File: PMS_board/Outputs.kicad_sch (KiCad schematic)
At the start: 92 parts, among them J10 AUX1, J11 AUX2, J12 D1, J13 D2, J14 D3, J15 D4, J16 T1, J17 T2, J18 T3, J19 T4, J4 Chopper_Shunt, J5 CORE, J6 DRIVE, J7 JET1, J8 JET2, J9 NET, Q5 NMOS, Q6 NMOS, U10 VN7140ASTR, U11 VN7140ASTR, U12 VN7140ASTR, U13 VN7007AHTR, U14 VN7007AHTR, U15 LM74700, U16 TLV7011DCKR, U17 LT1910, U19 LM74700, U25 IRFS7530TRL7PP

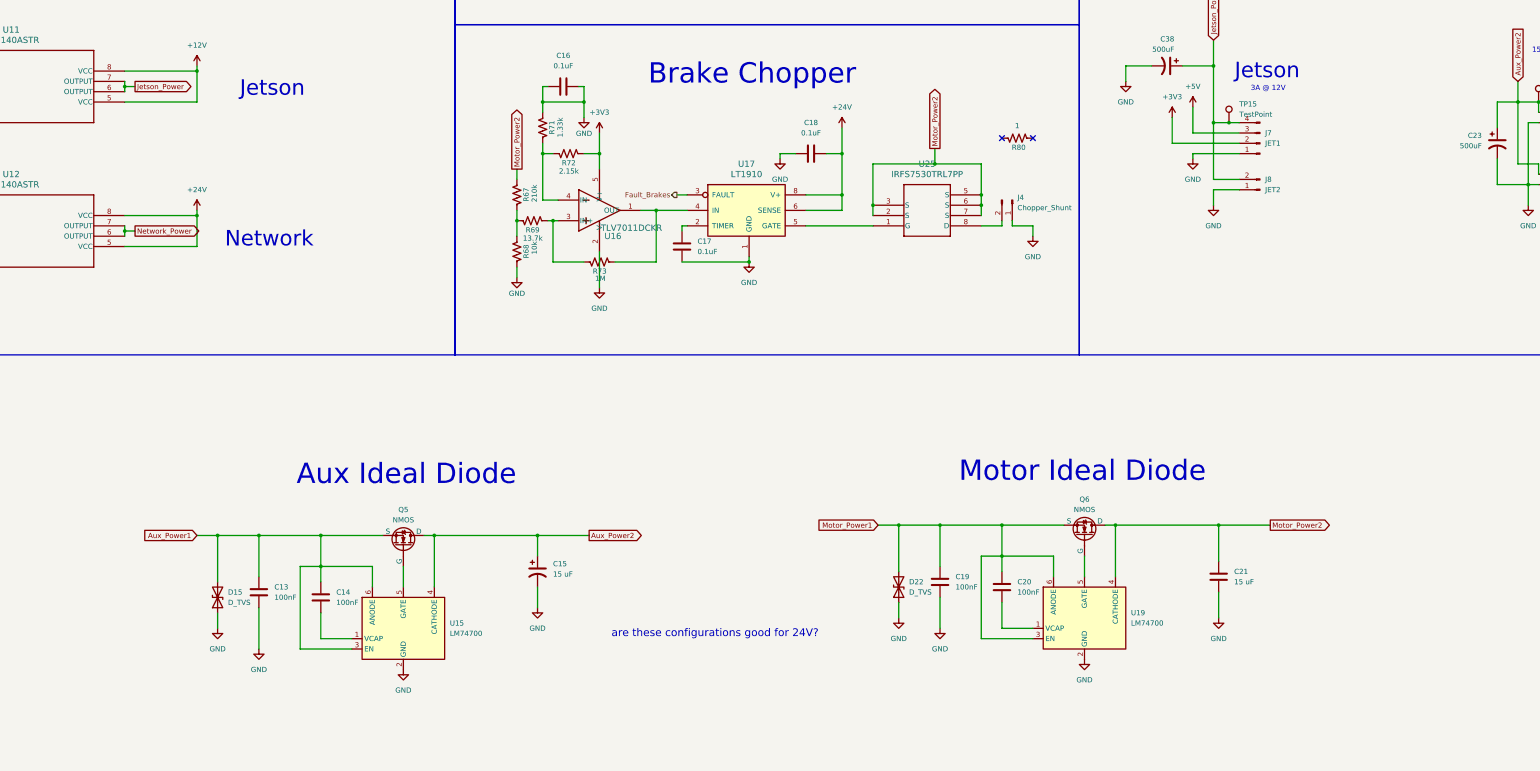
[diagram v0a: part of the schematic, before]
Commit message: Add pins to STM Chip
I also changed chips for jetson and motor out.
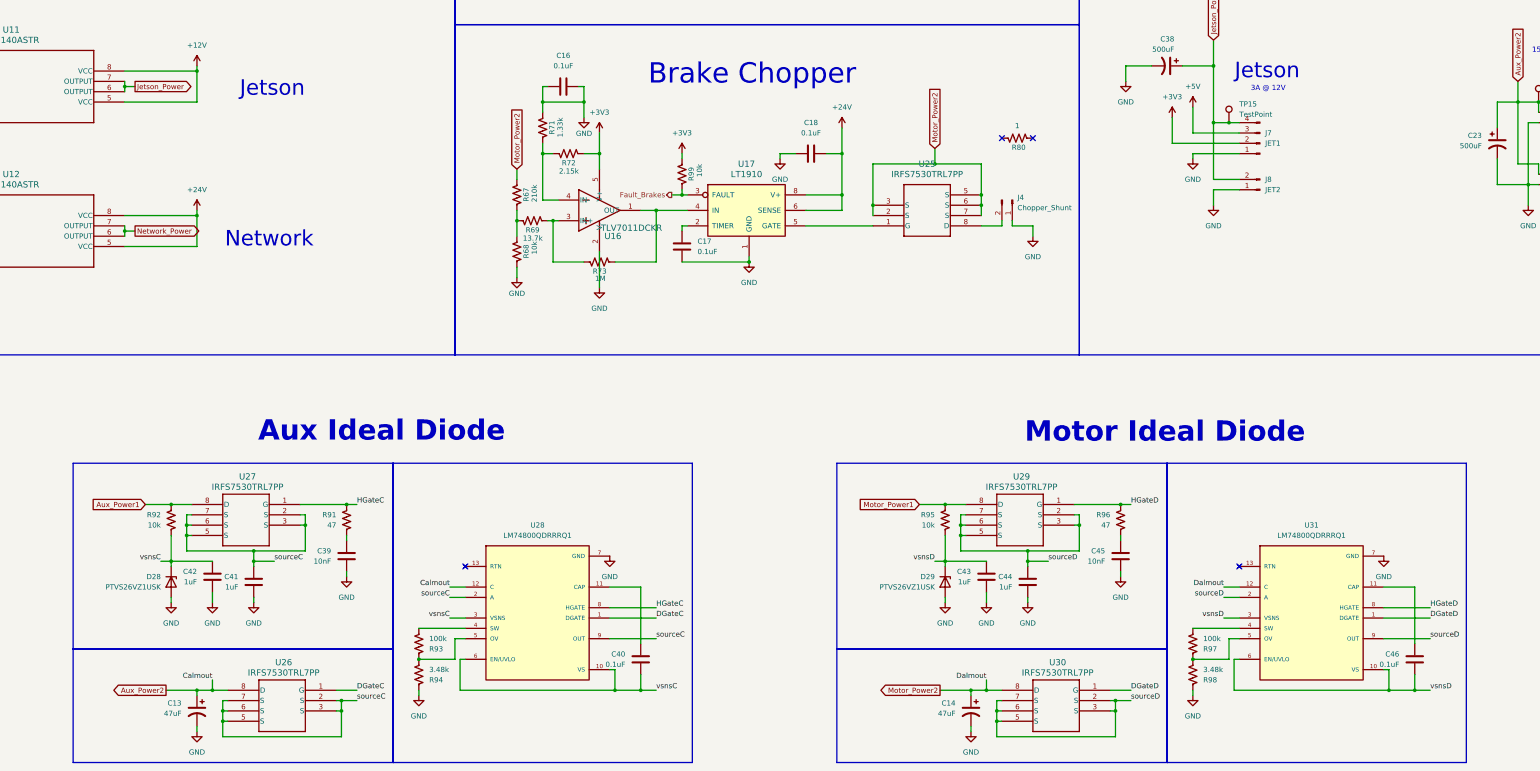
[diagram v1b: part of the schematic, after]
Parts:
- removed C13, C19: 100nF, Capacitor_SMD:C_0603_1608Metric, symbol Device:C
- removed C14, C20: 100nF, Capacitor_SMD:C_0603_1608Metric_Pad1.08x0.95mm_HandSolder, symbol Device:C
- removed C15: 15 uF, Capacitor_SMD:C_0603_1608Metric_Pad1.08x0.95mm_HandSolder, symbol Device:C_Polarized_US
- removed C21: 15 uF, Capacitor_SMD:C_0603_1608Metric_Pad1.08x0.95mm_HandSolder, symbol Device:C
- removed D15, D22: D_TVS, Diode_SMD:D_SOD-323_HandSoldering, symbol Device:D_TVS
- removed Q5, Q6: NMOS, Package_DFN_QFN:Nordic_AQFN-94-1EP_7x7mm_P0.4mm, symbol Simulation_SPICE:NMOS
- removed U15, U19: LM74700, Package_TO_SOT_SMD:SOT-23-6, symbol Power_Management:LM74700
- added C13, C14: 47uF, Capacitor_SMD:C_0603_1608Metric_Pad1.08x0.95mm_HandSolder, symbol Device:C_Polarized_US
- added C39, C45: 10nF, Capacitor_SMD:C_0603_1608Metric_Pad1.08x0.95mm_HandSolder, symbol Device:C
- added C40, C46: 0.1uF, Capacitor_SMD:C_0603_1608Metric_Pad1.08x0.95mm_HandSolder, symbol Device:C
- added C41, C42, C43, C44: 1uF, Capacitor_SMD:C_0603_1608Metric_Pad1.08x0.95mm_HandSolder, symbol Device:C
- added D28, D29: PTVS26VZ1USK, Diode_SMD:Nexperia_DSN1608-2_1.6x0.8mm, symbol Diode:PTVS26VZ1USK
- added R91, R96: 47, Resistor_SMD:R_0603_1608Metric_Pad0.98x0.95mm_HandSolder, symbol Device:R_US
- added R92, R95, R99: 10k, Resistor_SMD:R_0603_1608Metric_Pad0.98x0.95mm_HandSolder, symbol Device:R_US
- added R93, R97: 100k, Resistor_SMD:R_0603_1608Metric_Pad0.98x0.95mm_HandSolder, symbol Device:R_US
- added R94, R98: 3.48k, Resistor_SMD:R_0603_1608Metric_Pad0.98x0.95mm_HandSolder, symbol Device:R_US
- added U26, U27, U29, U30: IRFS7530TRL7PP, IRFS7530TRL7PP:PG-TO263-7_INF, symbol IRFS7530TRL7PP:IRFS7530TRL7PP
- added U28, U31: LM74800QDRRRQ1, LM74800QDRRRQ1:IC_LM74800QDRRRQ1, symbol LM74800QDRRRQ1:LM74800QDRRRQ1
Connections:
- net +3V3: now also R99.2
- net Aux_Power1: now also R92.2, U27.8 (D)
- net Aux_Power2: now also C13.1, U26.8 (D), U28.12 (C)
- net Fault_Brakes: now also R99.1
- net GND: now also C13.2, C14.2, C39.2, C41.2, C42.2, C43.2, C44.2, C45.2, D28.2 (A), D29.2 (A), R94.1, R98.1, U28.7 (GND), U31.7 (GND)
- net Motor_Power1: now also R95.2, U29.8 (D)
- net Motor_Power2: now also C14.1, U30.8 (D), U31.12 (C)
- new net: C40.1, U28.11 (CAP)
- new net: R93.2, U28.4 (SW)
- new net: R93.1, R94.2, U28.5 (OV)
- new net: C39.1, R91.2
- new net: R97.1, R98.2, U31.5 (OV)
- new net: R97.2, U31.4 (SW)
- new net: C46.1, U31.11 (CAP)
- new net: C45.1, R96.2
- new net DGateC: U26.1 (G), U28.1 (DGATE)
- new net DGateD: U30.1 (G), U31.1 (DGATE)
- new net HGateC: R91.1, U27.1 (G), U28.8 (HGATE)
- new net HGateD: R96.1, U29.1 (G), U31.8 (HGATE)
- new net sourceC: C41.1, U26.2 (S), U26.3 (S), U26.5 (S), U26.6 (S), U26.7 (S), U27.2 (S), U27.3 (S), U27.5 (S), U27.6 (S), U27.7 (S), U28.2 (A), U28.9 (OUT)
- new net sourceD: C44.1, U29.2 (S), U29.3 (S), U29.5 (S), U29.6 (S), U29.7 (S), U30.2 (S), U30.3 (S), U30.5 (S), U30.6 (S), U30.7 (S), U31.2 (A), U31.9 (OUT)
- new net vsnsC: C40.2, C42.1, D28.1 (K), R92.1, U28.10 (VS), U28.3 (VSNS), U28.6 (EN/UVLO)
- new net vsnsD: C43.1, C46.2, D29.1 (K), R95.1, U31.10 (VS), U31.3 (VSNS), U31.6 (EN/UVLO)
- no-connect marks 2 -> 4
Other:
- note removed: "are these configurations good for 24V?"

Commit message: Fix resistor value
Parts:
- R99: value 10k -> 4.7k
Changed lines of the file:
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@@
 			)
 		)
-		(property "Value" "10k"
+		(property "Value" "4.7k"
 			(at 278.638 170.18 90)
 			(show_name no)

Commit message: Schmitt Trigger
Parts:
- R67: value 210k -> 221k
- R69: value 13.7k -> 60.4k
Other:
- moved on the sheet: C14, U30
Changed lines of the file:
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@@
 	)
 	(junction
-		(at 381 304.8)
+		(at 379.73 304.8)
 		(diameter 0)
 		(color 0 0 0 0)
@@
 	)
 	(junction
-		(at 349.25 299.72)
+		(at 347.98 299.72)
 		(diameter 0)
 		(color 0 0 0 0)
@@
 	)
 	(junction
-		(at 345.44 299.72)
+		(at 344.17 299.72)
 		(diameter 0)
 		(color 0 0 0 0)
@@
 	)
 	(junction
-		(at 381 302.26)
+		(at 379.73 302.26)
 		(diameter 0)
 		(color 0 0 0 0)
@@
 	)
 	(junction
-		(at 351.79 304.8)
+		(at 350.52 304.8)
 		(diameter 0)
 		(color 0 0 0 0)
@@
 	)
 	(junction
-		(at 351.79 307.34)
+		(at 350.52 307.34)
 		(diameter 0)
 		(color 0 0 0 0)
@@
 	(wire
 		(pts
-			(xy 351.79 307.34) (xy 351.79 311.15)
+			(xy 350.52 307.34) (xy 350.52 311.15)
 		)
 		(stroke
@@
 	(wire
 		(pts
-			(xy 381 304.8) (xy 379.73 304.8)
+			(xy 379.73 304.8) (xy 378.46 304.8)
 		)
 		(stroke
@@
 	(wire
 		(pts
-			(xy 349.25 299.72) (xy 353.06 299.72)
+			(xy 347.98 299.72) (xy 351.79 299.72)
 		)
 		(stroke
@@
 	(wire
 		(pts
-			(xy 381 302.26) (xy 381 304.8)
+			(xy 379.73 302.26) (xy 379.73 304.8)
 		)
 		(stroke
@@
 	(wire
 		(pts
-			(xy 384.81 299.72) (xy 379.73 299.72)
+			(xy 383.54 299.72) (xy 378.46 299.72)
 		)
 		(stroke
@@
 	(wire
 		(pts
-			(xy 381 304.8) (xy 381 311.15)
+			(xy 379.73 304.8) (xy 379.73 311.15)
 		)
 		(stroke
@@
 	(wire
 		(pts
-			(xy 349.25 297.18) (xy 349.25 299.72)
+			(xy 347.98 297.18) (xy 347.98 299.72)
 		)
 		(stroke
@@
 	(wire
 		(pts
-			(xy 345.44 299.72) (xy 349.25 299.72)
+			(xy 344.17 299.72) (xy 347.98 299.72)
 		)
 		(stroke
@@
 	(wire
 		(pts
-			(xy 345.44 309.88) (xy 345.44 308.61)
+			(xy 344.17 309.88) (xy 344.17 308.61)
 		)
 		(stroke
@@
 	(wire
 		(pts
-			(xy 384.81 302.26) (xy 381 302.26)
+			(xy 383.54 302.26) (xy 379.73 302.26)
 		)
 		(stroke
@@
 	(wire
 		(pts
-			(xy 381 311.15) (xy 351.79 311.15)
+			(xy 379.73 311.15) (xy 350.52 311.15)
 		)
 		(stroke
@@
 	(wire
 		(pts
-			(xy 351.79 307.34) (xy 353.06 307.34)
+			(xy 350.52 307.34) (xy 351.79 307.34)
 		)
 		(stroke
@@
 	(wire
 		(pts
-			(xy 337.82 299.72) (xy 345.44 299.72)
+			(xy 336.55 299.72) (xy 344.17 299.72)
 		)
 		(stroke
@@
 	(wire
 		(pts
-			(xy 351.79 304.8) (xy 353.06 304.8)
+			(xy 350.52 304.8) (xy 351.79 304.8)
 		)
 		(stroke
@@
 	(wire
 		(pts
-			(xy 351.79 304.8) (xy 351.79 307.34)
+			(xy 350.52 304.8) (xy 350.52 307.34)
 		)
 		(stroke
@@
 	(wire
 		(pts
-			(xy 379.73 302.26) (xy 381 302.26)
+			(xy 378.46 302.26) (xy 379.73 302.26)
 		)
 		(stroke
@@
 	(wire
 		(pts
-			(xy 351.79 302.26) (xy 351.79 304.8)
+			(xy 350.52 302.26) (xy 350.52 304.8)
 		)
 		(stroke
@@
 	(wire
 		(pts
-			(xy 351.79 302.26) (xy 353.06 302.26)
+			(xy 350.52 302.26) (xy 351.79 302.26)
 		)
 		(stroke
@@
 	(wire
 		(pts
-			(xy 345.44 299.72) (xy 345.44 300.99)
+			(xy 344.17 299.72) (xy 344.17 300.99)
 		)
 		(stroke
@@
 	)
 	(label "DGateD"
-		(at 384.81 299.72 0)
+		(at 383.54 299.72 0)
 		(effects
 			(font
@@
 	)
 	(label "sourceD"
-		(at 384.81 302.26 0)
+		(at 383.54 302.26 0)
 		(effects
 			(font
@@
 	)
 	(label "Dalmout"
-		(at 349.25 297.18 180)
+		(at 347.98 297.18 180)
 		(effects
 			(font
@@
 	(global_label "Motor_Power2"
 		(shape output)
-		(at 337.82 299.72 180)
+		(at 336.55 299.72 180)
 		(fields_autoplaced yes)
 		(effects
@@
 		)
 		(property "Intersheetrefs" "${INTERSHEET_REFS}"
-			(at 321.7721 299.72 0)
+			(at 320.5021 299.72 0)
 			(hide yes)
 			(show_name no)
@@
 	(symbol
 		(lib_id "Device:C_Polarized_US")
-		(at 345.44 304.8 0)
+		(at 344.17 304.8 0)
 		(mirror y)
 		(unit 1)
@@
 		(fields_autoplaced yes)
 		(property "Reference" "C14"
-			(at 341.63 302.8949 0)
+			(at 340.36 302.8949 0)
 			(show_name no)
 			(do_not_autoplace no)
@@
 		)
 		(property "Value" "47uF"
-			(at 341.63 305.4349 0)
+			(at 340.36 305.4349 0)
 			(show_name no)
 			(do_not_autoplace no)
@@
 		)
 		(property "Footprint" "Capacitor_SMD:C_0603_1608Metric_Pad1.08x0.95mm_HandSolder"
-			(at 345.44 304.8 0)
+			(at 344.17 304.8 0)
 			(hide yes)
 			(show_name no)
@@
 		)
 		(property "Datasheet" ""
-			(at 345.44 304.8 0)
+			(at 344.17 304.8 0)
 			(hide yes)
 			(show_name no)
@@
 		)
 		(property "Description" "Polarized capacitor, US symbol"
-			(at 345.44 304.8 0)
+			(at 344.17 304.8 0)
 			(hide yes)
 			(show_name no)
@@
 		)
 		(property "KLC_S3.1" ""
-			(at 345.44 304.8 0)
+			(at 344.17 304.8 0)
 			(hide yes)
 			(show_name no)
@@
 		)
 		(property "KLC_S4.1" ""
-			(at 345.44 304.8 0)
+			(at 344.17 304.8 0)
 			(hide yes)
 			(show_name no)
@@
 		)
 		(property "KLC_S6.2" ""
-			(at 345.44 304.8 0)
+			(at 344.17 304.8 0)
 			(hide yes)
 			(show_name no)
@@
 			)
 		)
-		(property "Value" "13.7k"
+		(property "Value" "60.4k"
 			(at 240.03 188.468 90)
 			(show_name no)
@@
 			)
 		)
-		(property "Value" "210k"
+		(property "Value" "221k"
 			(at 237.998 175.26 90)
 			(show_name no)
@@
 		(lib_name "IRFS7530TRL7PP_1")
 		(lib_id "IRFS7530TRL7PP:IRFS7530TRL7PP")
-		(at 379.73 299.72 0)
+		(at 378.46 299.72 0)
 		(mirror y)
 		(unit 1)
@@
 		(fields_autoplaced yes)
 		(property "Reference" "U30"
-			(at 366.776 292.862 0)
+			(at 365.506 292.862 0)
 			(show_name no)
 			(do_not_autoplace no)
@@
 		)
 		(property "Value" "IRFS7530TRL7PP"
-			(at 366.776 295.402 0)
+			(at 365.506 295.402 0)
 			(show_name no)
 			(do_not_autoplace no)
@@
 		)
 		(property "Footprint" "IRFS7530TRL7PP:PG-TO263-7_INF"
-			(at 379.73 299.72 0)
+			(at 378.46 299.72 0)
 			(hide yes)
 			(show_name no)
@@
 		)
 		(property "Datasheet" "https://www.infineon.com/dgdl/irfs7530-7ppbf.pdf?fileId=5546d462533600a40153563a9d1e21d8"
-			(at 379.73 299.72 0)
+			(at 378.46 299.72 0)
 			(hide yes)
 			(show_name no)
@@
 		)
 		(property "Description" ""
-			(at 379.73 299.72 0)
+			(at 378.46 299.72 0)
 			(hide yes)
 			(show_name no)
@@
 		)
 		(property "KLC_S3.1" ""
-			(at 379.73 299.72 0)
+			(at 378.46 299.72 0)
 			(hide yes)
 			(show_name no)
@@
 		)
 		(property "KLC_S4.1" ""
-			(at 379.73 299.72 0)
+			(at 378.46 299.72 0)
 			(hide yes)
 			(show_name no)
@@
 		)
 		(property "KLC_S6.2" ""
-			(at 379.73 299.72 0)
+			(at 378.46 299.72 0)
 			(hide yes)
 			(show_name no)
@@
 	(symbol
 		(lib_id "power:GND")
-		(at 345.44 309.88 0)
+		(at 344.17 309.88 0)
 		(unit 1)
 		(body_style 1)
@@
 		(fields_autoplaced yes)
 		(property "Reference" "#PWR059"
-			(at 345.44 316.23 0)
+			(at 344.17 316.23 0)
 			(hide yes)
 			(show_name no)
@@
 		)
 		(property "Value" "GND"
-			(at 345.44 314.96 0)
+			(at 344.17 314.96 0)
 			(show_name no)
 			(do_not_autoplace no)
@@
 		)
 		(property "Footprint" ""
-			(at 345.44 309.88 0)
+			(at 344.17 309.88 0)
 			(hide yes)
 			(show_name no)
@@
 		)
 		(property "Datasheet" ""
-			(at 345.44 309.88 0)
+			(at 344.17 309.88 0)
 			(hide yes)
 			(show_name no)
@@
 		)
 		(property "Description" "Power symbol creates a global label with name \"GND\" , ground"
-			(at 345.44 309.88 0)
+			(at 344.17 309.88 0)
 			(hide yes)
 			(show_name no)
